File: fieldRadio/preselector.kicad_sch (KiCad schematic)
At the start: 54 parts, among them Q14 BSS123, Q15 BSS123, Q16 BSS123, Q17 BSS123, Q18 BSS123

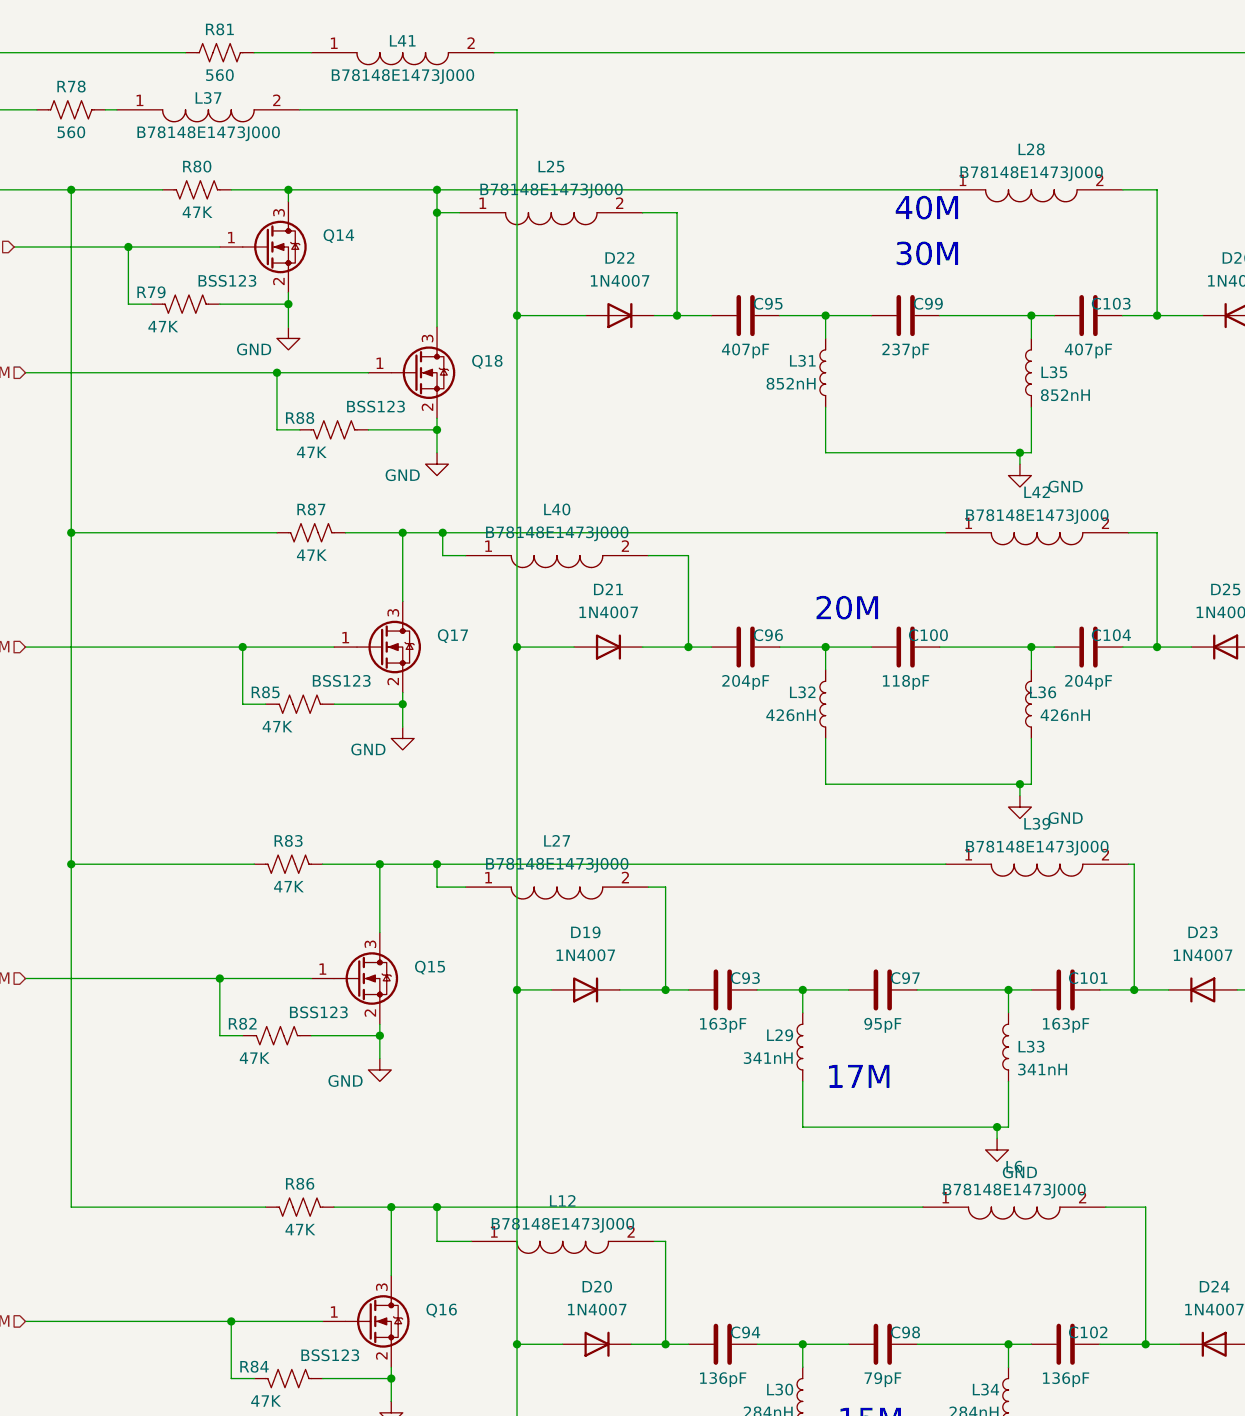
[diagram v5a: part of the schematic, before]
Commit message: Added support for unused gpio
Also added option for external clock generator.
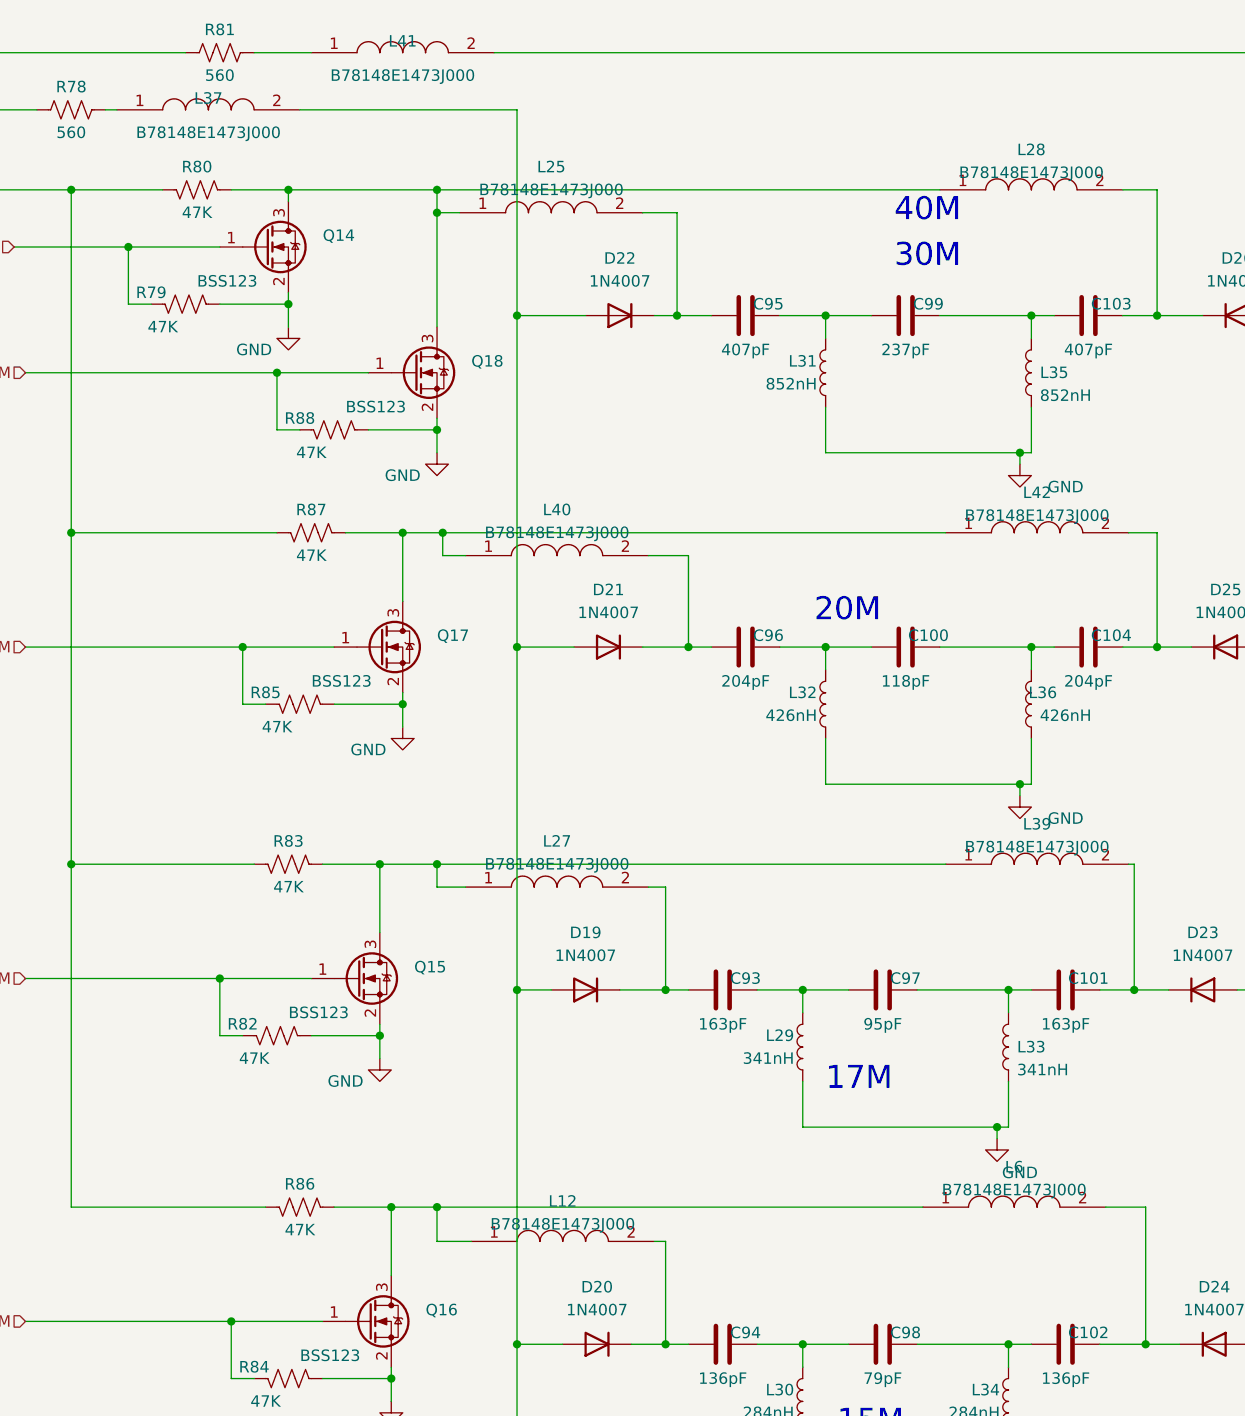
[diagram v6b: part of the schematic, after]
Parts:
- R78, R81: footprint Resistor_THT:R_Axial_DIN0617_L17.0mm_D6.0mm_P20.32mm_Horizontal -> Resistor_THT:R_Axial_DIN0207_L6.3mm_D2.5mm_P10.16mm_Horizontal
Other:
- moved on the sheet: L12, L25, L27, L28, L37, L39, L40, L41, L42, L6
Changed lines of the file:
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@@
       (effects (font (size 1.27 1.27)))
     )
-    (property "Footprint" "Resistor_THT:R_Axial_DIN0617_L17.0mm_D6.0mm_P20.32mm_Horizontal" (at 139.954 43.434 90)
+    (property "Footprint" "Resistor_THT:R_Axial_DIN0207_L6.3mm_D2.5mm_P10.16mm_Horizontal" (at 139.954 43.434 90)
       (effects (font (size 1.27 1.27)) hide)
     )
@@
       (effects (font (size 1.27 1.27)))
     )
-    (property "Footprint" "Resistor_THT:R_Axial_DIN0617_L17.0mm_D6.0mm_P20.32mm_Horizontal" (at 123.444 49.784 90)
-      (effects (font (size 1.27 1.27)) hide)
-    )
+    (property "Footprint" "Resistor_THT:R_Axial_DIN0207_L6.3mm_D2.5mm_P10.16mm_Horizontal" (at 123.444 49.784 90)
+      (effects (font (size 1.27 1.27)) hide)
+    )
